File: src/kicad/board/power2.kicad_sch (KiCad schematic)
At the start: 13 parts, among them J5 Conn_01x02_Male, J6 Conn_01x02_Male, Q1 DMG2305UX, U4 BQ25172

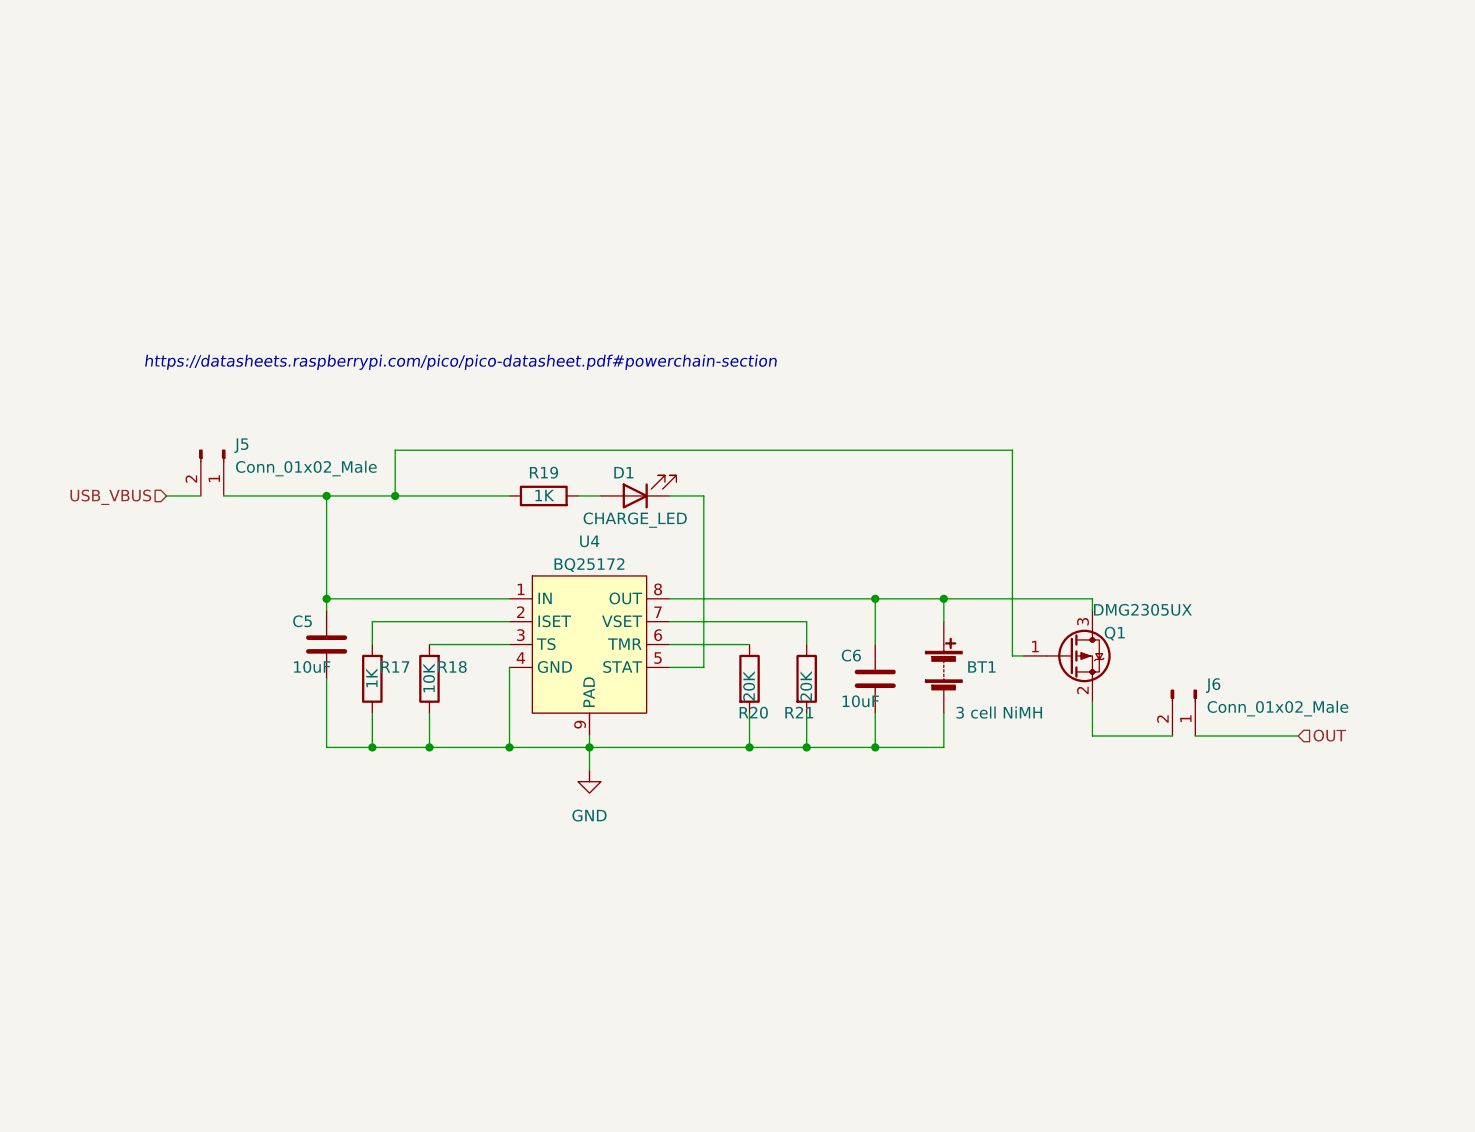
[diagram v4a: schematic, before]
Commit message: update with rp2040, instead of rpi pico. wip
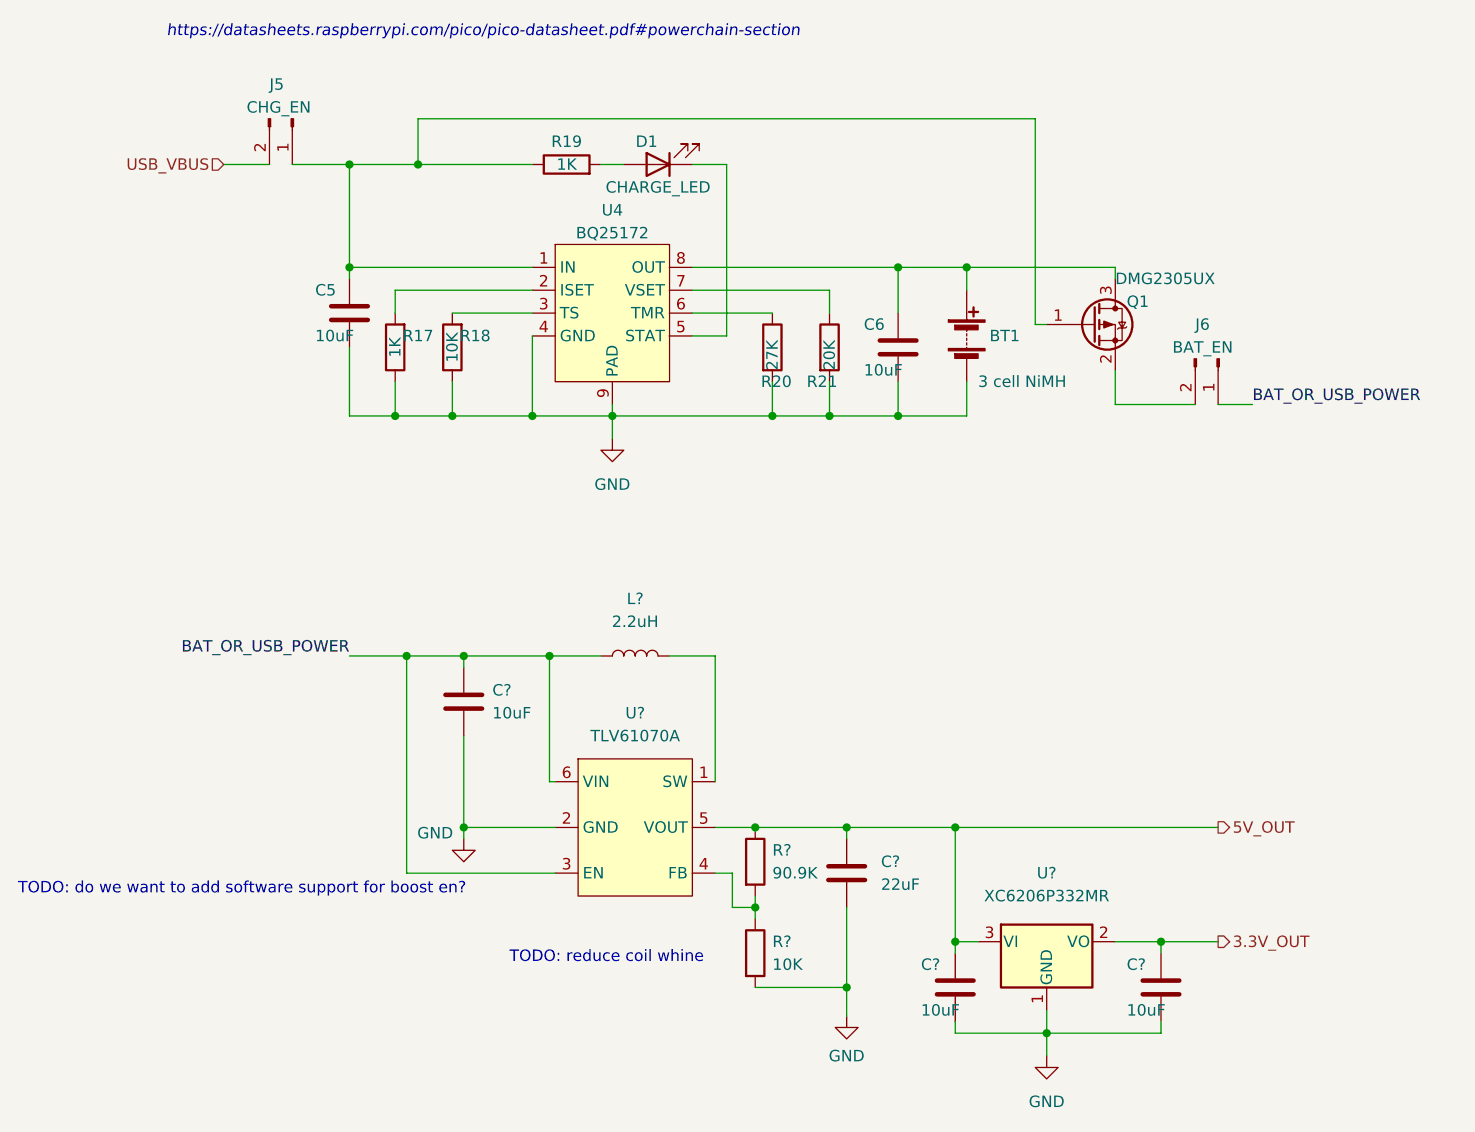
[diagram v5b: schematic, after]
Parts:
- added C? (x3): 10uF, Capacitor_SMD:C_0805_2012Metric, symbol Device:C
- added C?: 22uF, Capacitor_SMD:C_0805_2012Metric, symbol Device:C
- added L?: 2.2uH, Inductor_SMD:L_Sunlord_MWSA06xxS, symbol Device:L
- added R?: 10K, Resistor_SMD:R_0805_2012Metric, symbol Device:R
- added R?: 90.9K, Resistor_SMD:R_0805_2012Metric, symbol Device:R
- added U?: XC6206P332MR, Package_TO_SOT_SMD:SOT-23-3, symbol Regulator_Linear:XC6206PxxxMR
- added U?: TLV61070A, Package_SO:TSOP-6_1.65x3.05mm_P0.95mm, symbol project_library:TLV61070A
- J5: value Conn_01x02_Male -> CHG_EN
- J6: value Conn_01x02_Male -> BAT_EN
- R20: value 20K -> 27K; Vendor C4328 -> (none)
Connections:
- net GND: now also C?.2, C?.2, C?.2, C?.2, R?.2, U?.1 (GND), U?.2 (GND)
- net OUT renamed BAT_OR_USB_POWER
- net BAT_OR_USB_POWER: now also C?.1, L?.1, U?.3 (EN), U?.6 (VIN)
- new net: R?.1, R?.2, U?.4 (FB)
- new net: L?.2, U?.1 (SW)
- new net 3.3V_OUT: C?.1, U?.2 (VO)
- new net 5V_OUT: C?.1, C?.1, R?.1, U?.3 (VI), U?.5 (VOUT)
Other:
- note added: "TODO: do we want to add software support for boost en?"
- note added: "TODO: reduce coil whine"
- moved on the sheet: BT1, C5, C6, D1, J5, J6, Q1, R17, R18, R19, R20, R21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
